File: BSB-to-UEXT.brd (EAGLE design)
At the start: 51 x 28 mm, 24 parts, among them Q1 BC847, Q2 BC857

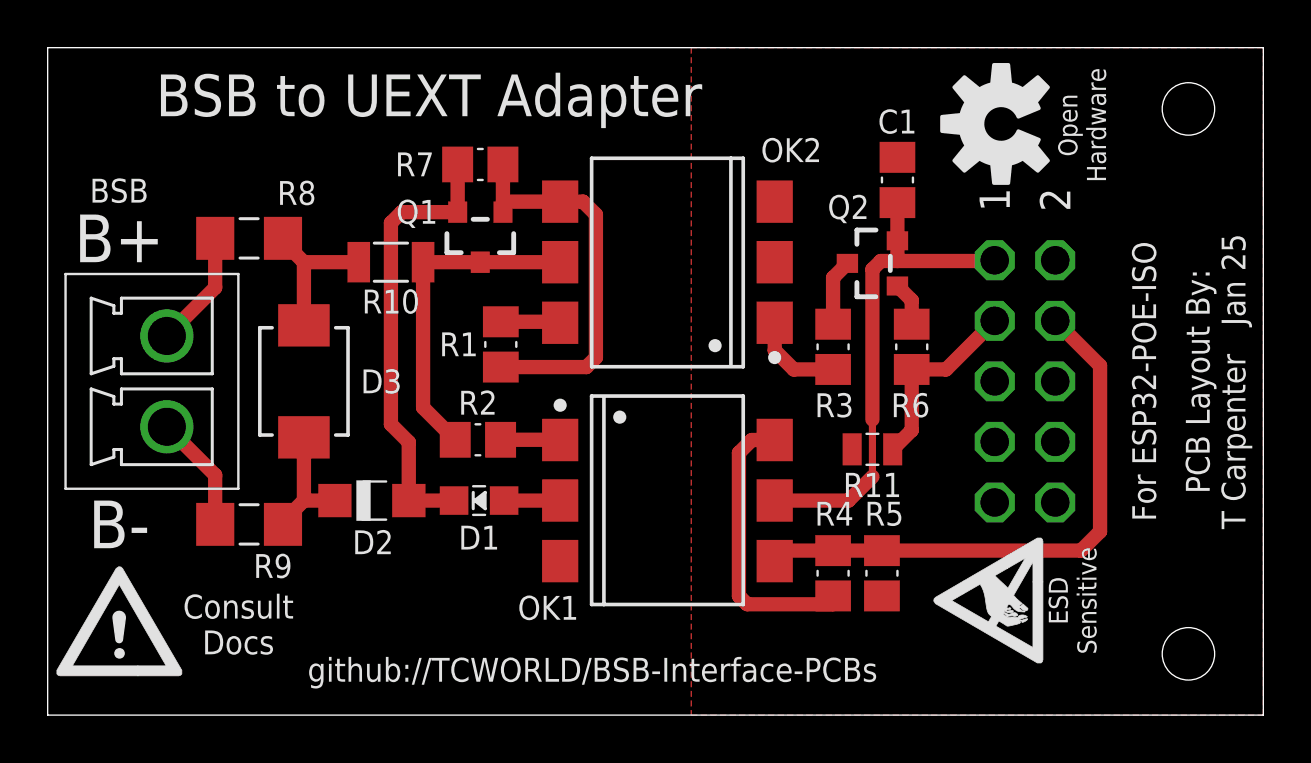
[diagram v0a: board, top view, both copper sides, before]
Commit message: Change BSB-to-UEXT Tx Pin Assignment
Follow the BSB-LAN repo in moving TX onto the UEXT-SSEL pin instead of the UEXT-TX pin. This is done to avoid issues with the TX pin needing to be pulled low during the boot phase, but that in turn would "short" out the BSB bus until everything is booted up.
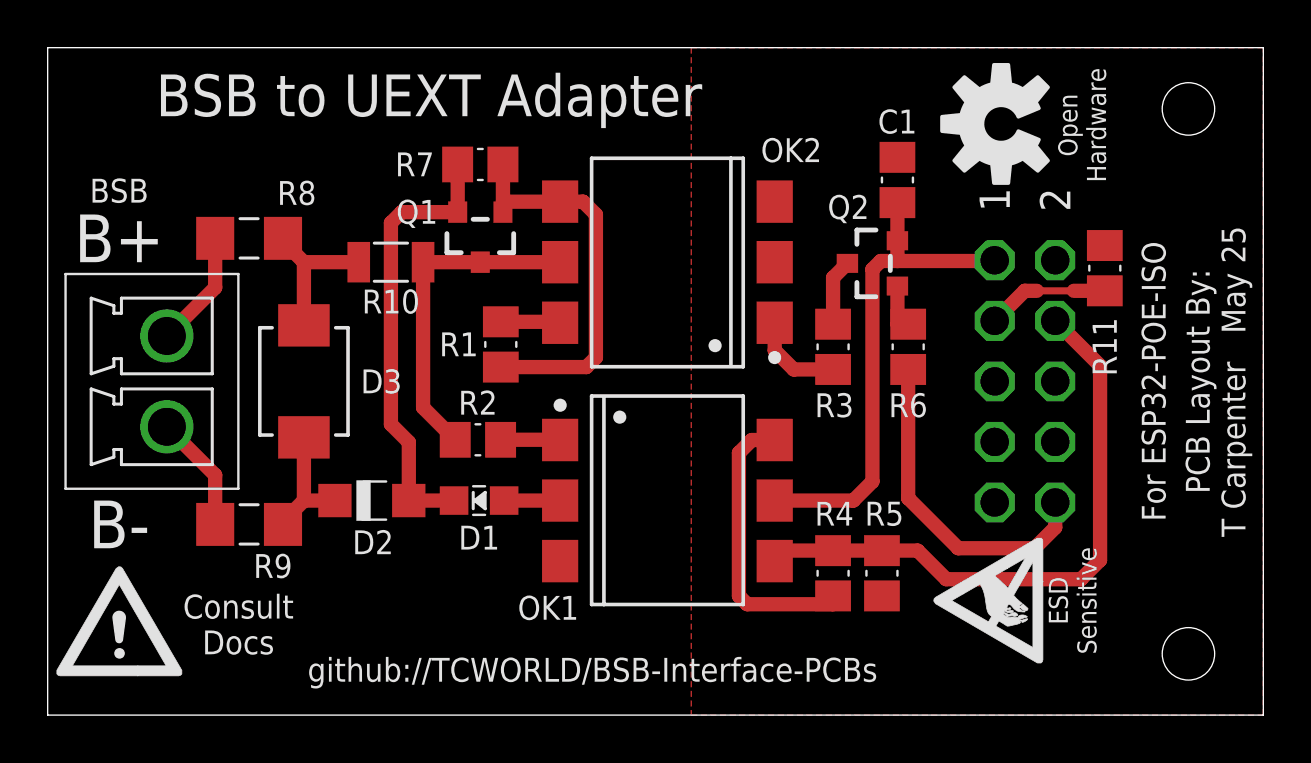
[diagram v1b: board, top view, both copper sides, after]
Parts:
- R11: device BSB-LAN:R0805L -> BSB-LAN:R0805
- moved R11 12.4 mm to (44.4, 18.8), turned to 90 degrees
- moved R6 0.15 mm to (36.1, 15.4)
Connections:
- net SSEL: now also R6.2
- net TXD: no longer R6.2
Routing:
- net SSEL: track 0.00 -> 13.9 mm
- net TXD: track 8.01 -> 5.14 mm
- net RXD: track 24.0 -> 25.7 mm
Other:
- board text added: "PCB Layout By: T Carpenter May 25"
- board text removed: "PCB Layout By: T Carpenter Jan 25"
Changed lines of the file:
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@@
 <layer number="14" name="Route14" color="1" fill="6" visible="no" active="no"/>
 <layer number="15" name="Route15" color="4" fill="6" visible="no" active="no"/>
-<layer number="16" name="Bottom" color="1" fill="1" visible="yes" active="yes"/>
+<layer number="16" name="Bottom" color="1" fill="1" visible="no" active="yes"/>
 <layer number="17" name="Pads" color="2" fill="1" visible="yes" active="yes"/>
 <layer number="18" name="Vias" color="2" fill="1" visible="yes" active="yes"/>
@@
 <layer number="20" name="Dimension" color="15" fill="1" visible="yes" active="yes"/>
 <layer number="21" name="tPlace" color="7" fill="1" visible="yes" active="yes"/>
-<layer number="22" name="bPlace" color="7" fill="1" visible="yes" active="yes"/>
+<layer number="22" name="bPlace" color="7" fill="1" visible="no" active="yes"/>
 <layer number="23" name="tOrigins" color="15" fill="1" visible="yes" active="yes"/>
-<layer number="24" name="bOrigins" color="15" fill="1" visible="yes" active="yes"/>
+<layer number="24" name="bOrigins" color="15" fill="1" visible="no" active="yes"/>
 <layer number="25" name="tNames" color="7" fill="1" visible="yes" active="yes"/>
-<layer number="26" name="bNames" color="7" fill="1" visible="yes" active="yes"/>
+<layer number="26" name="bNames" color="7" fill="1" visible="no" active="yes"/>
 <layer number="27" name="tValues" color="7" fill="1" visible="no" active="yes"/>
 <layer number="28" name="bValues" color="7" fill="1" visible="no" active="yes"/>
 <layer number="29" name="tStop" color="7" fill="3" visible="yes" active="yes"/>
-<layer number="30" name="bStop" color="7" fill="6" visible="yes" active="yes"/>
+<layer number="30" name="bStop" color="7" fill="6" visible="no" active="yes"/>
 <layer number="31" name="tCream" color="7" fill="4" visible="no" active="yes"/>
 <layer number="32" name="bCream" color="7" fill="5" visible="no" active="yes"/>
@@
 <layer number="38" name="bTest" color="7" fill="1" visible="no" active="yes"/>
 <layer number="39" name="tKeepout" color="4" fill="11" visible="yes" active="yes"/>
-<layer number="40" name="bKeepout" color="1" fill="11" visible="yes" active="yes"/>
+<layer number="40" name="bKeepout" color="1" fill="11" visible="no" active="yes"/>
 <layer number="41" name="tRestrict" color="4" fill="10" visible="yes" active="yes"/>
-<layer number="42" name="bRestrict" color="1" fill="10" visible="yes" active="yes"/>
+<layer number="42" name="bRestrict" color="1" fill="10" visible="no" active="yes"/>
 <layer number="43" name="vRestrict" color="2" fill="10" visible="no" active="yes"/>
 <layer number="44" name="Drills" color="7" fill="1" visible="no" active="yes"/>
-<layer number="45" name="Holes" color="7" fill="1" visible="yes" active="yes"/>
+<layer number="45" name="Holes" color="7" fill="1" visible="no" active="yes"/>
 <layer number="46" name="Milling" color="3" fill="1" visible="no" active="yes"/>
 <layer number="47" name="Measures" color="7" fill="1" visible="no" active="yes"/>
-<layer number="48" name="Document" color="7" fill="1" visible="yes" active="yes"/>
+<layer number="48" name="Document" color="7" fill="1" visible="no" active="yes"/>
 <layer number="49" name="Reference" color="7" fill="1" visible="no" active="yes"/>
 <layer number="50" name="dxf" color="7" fill="1" visible="no" active="no"/>
@@
 <text x="16" y="26" size="1.75" layer="21" font="vector" ratio="15" align="center">BSB to UEXT Adapter</text>
 <text x="49" y="14" size="1" layer="21" font="vector" ratio="15" rot="R90" align="center">PCB Layout By:
-T Carpenter   Jan 25</text>
+T Carpenter   May 25</text>
 <text x="8" y="3.8" size="1" layer="21" font="vector" ratio="15" align="center">Consult
 Docs</text>
-<text x="46" y="14" size="1" layer="21" font="vector" ratio="15" rot="R90" align="center">For ESP32-POE-ISO</text>
+<text x="46.4" y="14" size="1" layer="21" font="vector" ratio="15" rot="R90" align="center">For ESP32-POE-ISO</text>
 <text x="10.9" y="1.9" size="1" layer="21" font="vector" ratio="15" align="center-left">github://TCWORLD/BSB-Interface-PCBs</text>
 <text x="7" y="26" size="1" layer="22" font="vector" ratio="15" rot="MR180" align="center">JLCJLCJLC</text>
@@
 <attribute name="LCSC_PART" value="C17629" x="32.95" y="5.95" size="1.778" layer="27" rot="R270" display="off"/>
 </element>
-<element name="R6" library="BSB-LAN" package="R0805" value="4.7k" x="36.25" y="15.45" smashed="yes" rot="R270">
-<attribute name="NAME" x="36.2" y="13" size="1" layer="25" font="vector" ratio="15" rot="R180" align="center"/>
-<attribute name="LCSC_PART" value="C17673" x="36.25" y="15.45" size="1.778" layer="27" rot="R270" display="off"/>
+<element name="R6" library="BSB-LAN" package="R0805" value="4.7k" x="36.1" y="15.45" smashed="yes" rot="R270">
+<attribute name="NAME" x="36.1" y="13" size="1" layer="25" font="vector" ratio="15" align="center"/>
+<attribute name="LCSC_PART" value="C17673" x="36.1" y="15.45" size="1.778" layer="27" rot="R270" display="off"/>
 </element>
 <element name="R5" library="BSB-LAN" package="R0805" value="4.7k" x="35" y="5.95" smashed="yes" rot="R270">
@@
 <attribute name="VALUE" value="DNI" x="40" y="24.8" size="1.778" layer="27" rot="R90" display="off"/>
 </element>
-<element name="R11" library="BSB-LAN" package="R0805L" value="4.7k" x="34.6" y="11.15" smashed="yes" rot="R180">
-<attribute name="LCSC_PART" value="C17673" x="34.6" y="11.15" size="1" layer="27" font="vector" ratio="15" rot="R180" display="off"/>
-<attribute name="NAME" x="34.6" y="9.655" size="1.016" layer="25" font="vector" ratio="15" align="center"/>
-<attribute name="VALUE" x="34.6" y="13.055" size="1.016" layer="27" font="vector" ratio="15" rot="R180" align="center"/>
+<element name="R11" library="BSB-LAN" package="R0805" value="4.7k" x="44.35" y="18.75" smashed="yes" rot="R90">
+<attribute name="LCSC_PART" value="C17673" x="44.35" y="18.75" size="1" layer="27" font="vector" ratio="15" rot="R90" display="off"/>
+<attribute name="NAME" x="44.345" y="15.45" size="1.016" layer="25" font="vector" ratio="15" rot="R90" align="center"/>
+<attribute name="VALUE" x="46.255" y="18.75" size="1.016" layer="27" font="vector" ratio="15" rot="R90" align="center"/>
 </element>
 </elements>
@@
 <wire x1="35.65" y1="19.05" x2="34.95" y2="19.05" width="0.6" layer="1"/>
 <wire x1="34.95" y1="19.05" x2="34.6" y2="18.7" width="0.6" layer="1"/>
-<wire x1="34.6" y1="18.7" x2="34.6" y2="12.4" width="0.6" layer="1"/>
-<wire x1="34.6" y1="12.4" x2="34.6" y2="10" width="0.3" layer="1"/>
-<wire x1="34.6" y1="10" x2="33.6" y2="9" width="0.6" layer="1"/>
-<wire x1="30.5" y1="9" x2="33.6" y2="9" width="0.6" layer="1"/>
+<wire x1="34.6" y1="18.7" x2="34.6" y2="9.8" width="0.6" layer="1"/>
+<wire x1="30.5" y1="9" x2="33.8" y2="9" width="0.6" layer="1"/>
+<wire x1="33.8" y1="9" x2="34.6" y2="9.8" width="0.6" layer="1"/>
 <wire x1="35.65" y1="19.9" x2="35.65" y2="21.5" width="0.6" layer="1"/>
 <wire x1="39.73" y1="19.08" x2="39.73" y2="19.05" width="0.6" layer="1"/>
@@
 </signal>
 <signal name="TXD">
-<contactref element="R6" pad="2"/>
 <contactref element="UEXT" pad="3"/>
+<wire x1="40.99" y1="17.8" x2="39.73" y2="16.54" width="0.6" layer="1"/>
 <contactref element="R11" pad="1"/>
-<wire x1="36.25" y1="14.5" x2="36.25" y2="11.95" width="0.6" layer="1"/>
-<wire x1="36.25" y1="11.95" x2="35.45" y2="11.15" width="0.6" layer="1"/>
-<wire x1="36.25" y1="14.5" x2="37.69" y2="14.5" width="0.6" layer="1"/>
-<wire x1="37.69" y1="14.5" x2="39.73" y2="16.54" width="0.6" layer="1"/>
+<wire x1="40.99" y1="17.8" x2="41.5" y2="17.8" width="0.6" layer="1"/>
+<wire x1="41.5" y1="17.8" x2="43.05" y2="17.8" width="0.3" layer="1"/>
+<wire x1="43.05" y1="17.8" x2="44.35" y2="17.8" width="0.6" layer="1"/>
 </signal>
 <signal name="TXD-B">
 <contactref element="R6" pad="1"/>
 <contactref element="Q2" pad="B"/>
-<wire x1="35.65" y1="18" x2="36.25" y2="17.4" width="0.6" layer="1"/>
-<wire x1="36.25" y1="17.4" x2="36.25" y2="16.4" width="0.6" layer="1"/>
+<wire x1="35.65" y1="18" x2="35.65" y2="16.4" width="0.6" layer="1"/>
+<wire x1="35.65" y1="16.4" x2="36.1" y2="16.4" width="0.6" layer="1"/>
 </signal>
 <signal name="RXD-B">
@@
 <wire x1="30.5" y1="6.9" x2="32.95" y2="6.9" width="0.6" layer="1"/>
 <wire x1="32.95" y1="6.9" x2="35" y2="6.9" width="0.6" layer="1"/>
-<wire x1="35" y1="6.9" x2="43.35" y2="6.9" width="0.6" layer="1"/>
-<wire x1="43.35" y1="6.9" x2="44.15" y2="7.7" width="0.6" layer="1"/>
+<wire x1="35" y1="6.9" x2="36.5" y2="6.9" width="0.6" layer="1"/>
+<wire x1="36.5" y1="6.9" x2="37.7" y2="5.7" width="0.6" layer="1"/>
+<wire x1="37.7" y1="5.7" x2="43.35" y2="5.7" width="0.6" layer="1"/>
+<wire x1="43.35" y1="5.7" x2="44.15" y2="6.5" width="0.6" layer="1"/>
 <wire x1="42.27" y1="16.54" x2="44.15" y2="14.66" width="0.6" layer="1"/>
-<wire x1="44.15" y1="14.66" x2="44.15" y2="7.7" width="0.6" layer="1"/>
+<wire x1="44.15" y1="14.66" x2="44.15" y2="6.5" width="0.6" layer="1"/>
 </signal>
 <signal name="BSB-RX-K">
@@
 <signal name="SSEL">
 <contactref element="UEXT" pad="10"/>
+<contactref element="R6" pad="2"/>
+<wire x1="36.1" y1="14.5" x2="36.1" y2="9.1" width="0.6" layer="1"/>
+<wire x1="42.27" y1="8.92" x2="42.27" y2="7.87" width="0.6" layer="1"/>
+<wire x1="42.27" y1="7.87" x2="41.4" y2="7" width="0.6" layer="1"/>
+<wire x1="41.4" y1="7" x2="38.2" y2="7" width="0.6" layer="1"/>
+<wire x1="38.2" y1="7" x2="36.1" y2="9.1" width="0.6" layer="1"/>
 </signal>
 <signal name="TVS-BSB+">
